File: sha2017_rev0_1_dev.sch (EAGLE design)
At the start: 79 parts, among them IC1 CP210X_USB_UART, IC2 AP7215, IC32 ESP32_AI, Q1 MMBT2222A, Q2 MMBT2222A, Q6 MOSFET-NCHANNELBSS123LT1G, SW801 MCMT5-F-V, X701 2908-05WB-MG

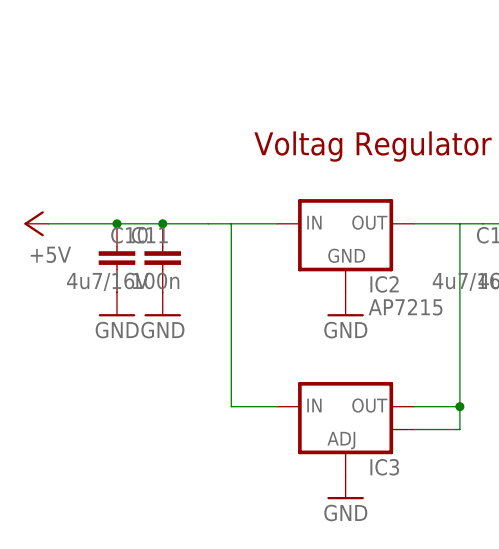
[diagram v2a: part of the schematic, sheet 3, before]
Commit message: all parts places minor adjustments needed
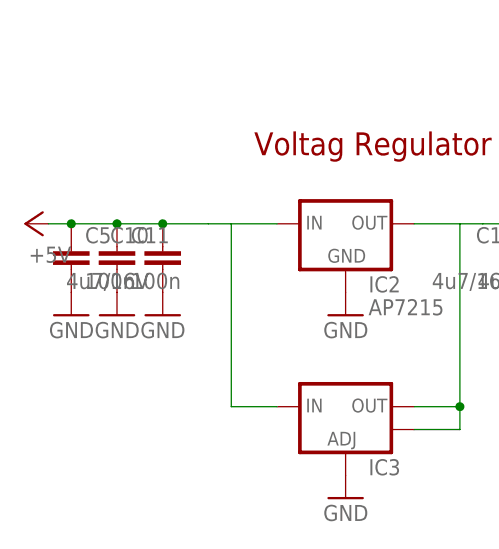
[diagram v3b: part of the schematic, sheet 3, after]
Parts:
- added C5: 100n, rcl:C-EUC0805
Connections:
- net +5V: now also C5.1
- net GND: now also C5.2
- net LCD_!RESET: now also SJ8.2; no longer SJ12.2
- net LCD_BUSY: now also SJ12.2; no longer SJ14.2
- net LCD_CS: now also SJ9.2; no longer SJ11.2
- net LCD_D/!S: now also SJ14.2; no longer SJ8.2
- net LCD_MOSI: now also SJ11.2; no longer SJ9.2
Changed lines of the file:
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@@
 <part name="GND15" library="supply1" deviceset="GND" device=""/>
 <part name="VDD5" library="supply1" deviceset="VDD" device=""/>
+<part name="C5" library="rcl" deviceset="C-EU" device="C0805" value="100n"/>
+<part name="GND14" library="supply1" deviceset="GND" device=""/>
 </parts>
 <sheets>
@@
 </segment>
 </net>
-<net name="LCD_D/!S" class="0">
-<segment>
-<label x="228.6" y="160.02" size="1.27" layer="95" xref="yes"/>
-<pinref part="SJ8" gate="G$1" pin="2"/>
-<wire x1="223.52" y1="160.02" x2="228.6" y2="160.02" width="0.1524" layer="91"/>
-</segment>
-</net>
-<net name="LCD_MOSI" class="0">
+<net name="LCD_SCK" class="0">
+<segment>
+<wire x1="218.44" y1="152.4" x2="228.6" y2="152.4" width="0.1524" layer="91"/>
+<label x="228.6" y="152.4" size="1.27" layer="95" xref="yes"/>
+<pinref part="SJ10" gate="G$1" pin="2"/>
+</segment>
+</net>
+<net name="LCD_CS" class="0">
 <segment>
 <label x="228.6" y="154.94" size="1.27" layer="95" xref="yes"/>
 <pinref part="SJ9" gate="G$1" pin="2"/>
 <wire x1="223.52" y1="154.94" x2="228.6" y2="154.94" width="0.1524" layer="91"/>
-</segment>
-</net>
-<net name="LCD_SCK" class="0">
-<segment>
-<wire x1="218.44" y1="152.4" x2="228.6" y2="152.4" width="0.1524" layer="91"/>
-<label x="228.6" y="152.4" size="1.27" layer="95" xref="yes"/>
-<pinref part="SJ10" gate="G$1" pin="2"/>
-</segment>
-</net>
-<net name="LCD_CS" class="0">
-<segment>
-<label x="228.6" y="149.86" size="1.27" layer="95" xref="yes"/>
-<pinref part="SJ11" gate="G$1" pin="2"/>
-<wire x1="223.52" y1="149.86" x2="228.6" y2="149.86" width="0.1524" layer="91"/>
 </segment>
 </net>
@@
 <net name="LCD_BUSY" class="0">
 <segment>
+<pinref part="SJ12" gate="G$1" pin="2"/>
+<wire x1="218.44" y1="162.56" x2="228.6" y2="162.56" width="0.1524" layer="91"/>
+<label x="228.6" y="162.56" size="1.27" layer="95" xref="yes"/>
+</segment>
+</net>
+<net name="LCD_!RESET" class="0">
+<segment>
+<label x="228.6" y="160.02" size="1.27" layer="95" xref="yes"/>
+<pinref part="SJ8" gate="G$1" pin="2"/>
+<wire x1="223.52" y1="160.02" x2="228.6" y2="160.02" width="0.1524" layer="91"/>
+</segment>
+</net>
+<net name="LCD_D/!S" class="0">
+<segment>
 <pinref part="SJ14" gate="G$1" pin="2"/>
 <wire x1="218.44" y1="157.48" x2="228.6" y2="157.48" width="0.1524" layer="91"/>
@@
 </segment>
 </net>
-<net name="LCD_!RESET" class="0">
-<segment>
-<pinref part="SJ12" gate="G$1" pin="2"/>
-<wire x1="218.44" y1="162.56" x2="228.6" y2="162.56" width="0.1524" layer="91"/>
-<label x="228.6" y="162.56" size="1.27" layer="95" xref="yes"/>
+<net name="LCD_MOSI" class="0">
+<segment>
+<label x="228.6" y="149.86" size="1.27" layer="95" xref="yes"/>
+<pinref part="SJ11" gate="G$1" pin="2"/>
+<wire x1="223.52" y1="149.86" x2="228.6" y2="149.86" width="0.1524" layer="91"/>
 </segment>
 </net>
@@
 <instance part="IC3" gate="G$1" x="157.48" y="119.38"/>
 <instance part="GND1" gate="1" x="157.48" y="109.22" rot="MR0"/>
+<instance part="C5" gate="G$1" x="127" y="137.16"/>
+<instance part="GND14" gate="1" x="127" y="129.54" rot="MR0"/>
 </instances>
 <busses>
@@
 <pinref part="IC3" gate="G$1" pin="ADJ"/>
 <pinref part="GND1" gate="1" pin="GND"/>
+</segment>
+<segment>
+<pinref part="C5" gate="G$1" pin="2"/>
+<pinref part="GND14" gate="1" pin="GND"/>
 </segment>
 </net>
@@
 <junction x="137.16" y="139.7"/>
 <pinref part="C11" gate="G$1" pin="1"/>
-<wire x1="132.08" y1="139.7" x2="124.46" y2="139.7" width="0.1524" layer="91"/>
+<wire x1="132.08" y1="139.7" x2="127" y2="139.7" width="0.1524" layer="91"/>
 <junction x="132.08" y="139.7"/>
+<wire x1="127" y1="139.7" x2="124.46" y2="139.7" width="0.1524" layer="91"/>
 <wire x1="142.24" y1="139.7" x2="144.78" y2="139.7" width="0.1524" layer="91"/>
 <pinref part="IC2" gate="G$1" pin="IN"/>
@@
 <pinref part="IC3" gate="G$1" pin="IN"/>
 <wire x1="144.78" y1="119.38" x2="149.86" y2="119.38" width="0.1524" layer="91"/>
-</segment>
-</net>
+<pinref part="C5" gate="G$1" pin="1"/>
+<junction x="127" y="139.7"/>
+</segment>
+</net>

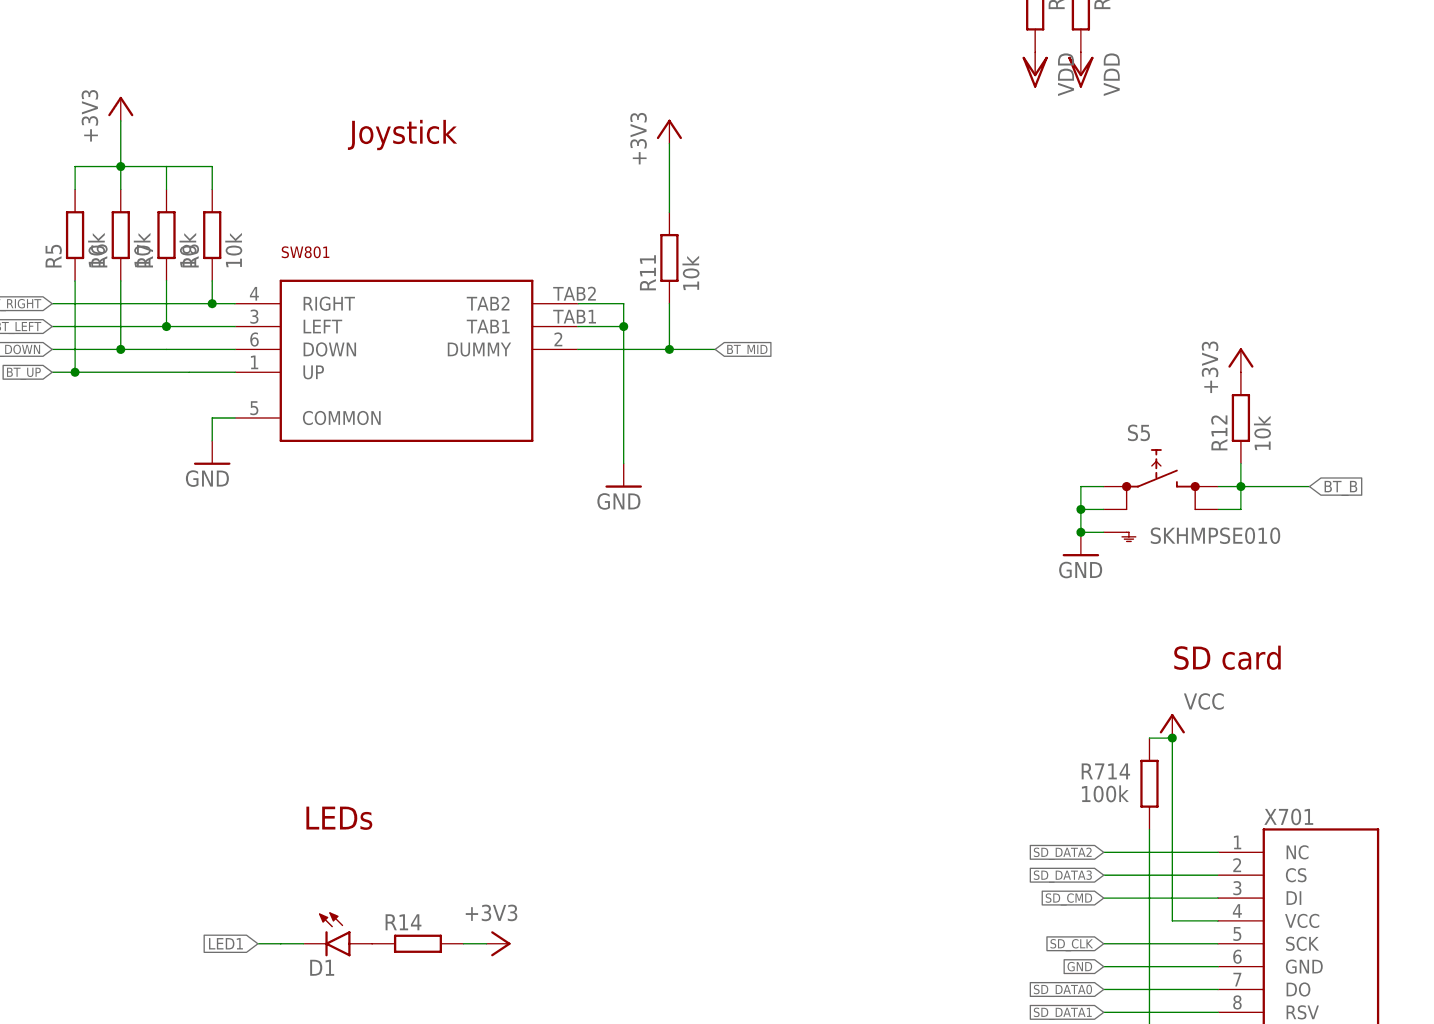
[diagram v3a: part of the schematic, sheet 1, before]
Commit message: finished routing. Part designators needs to be fixed
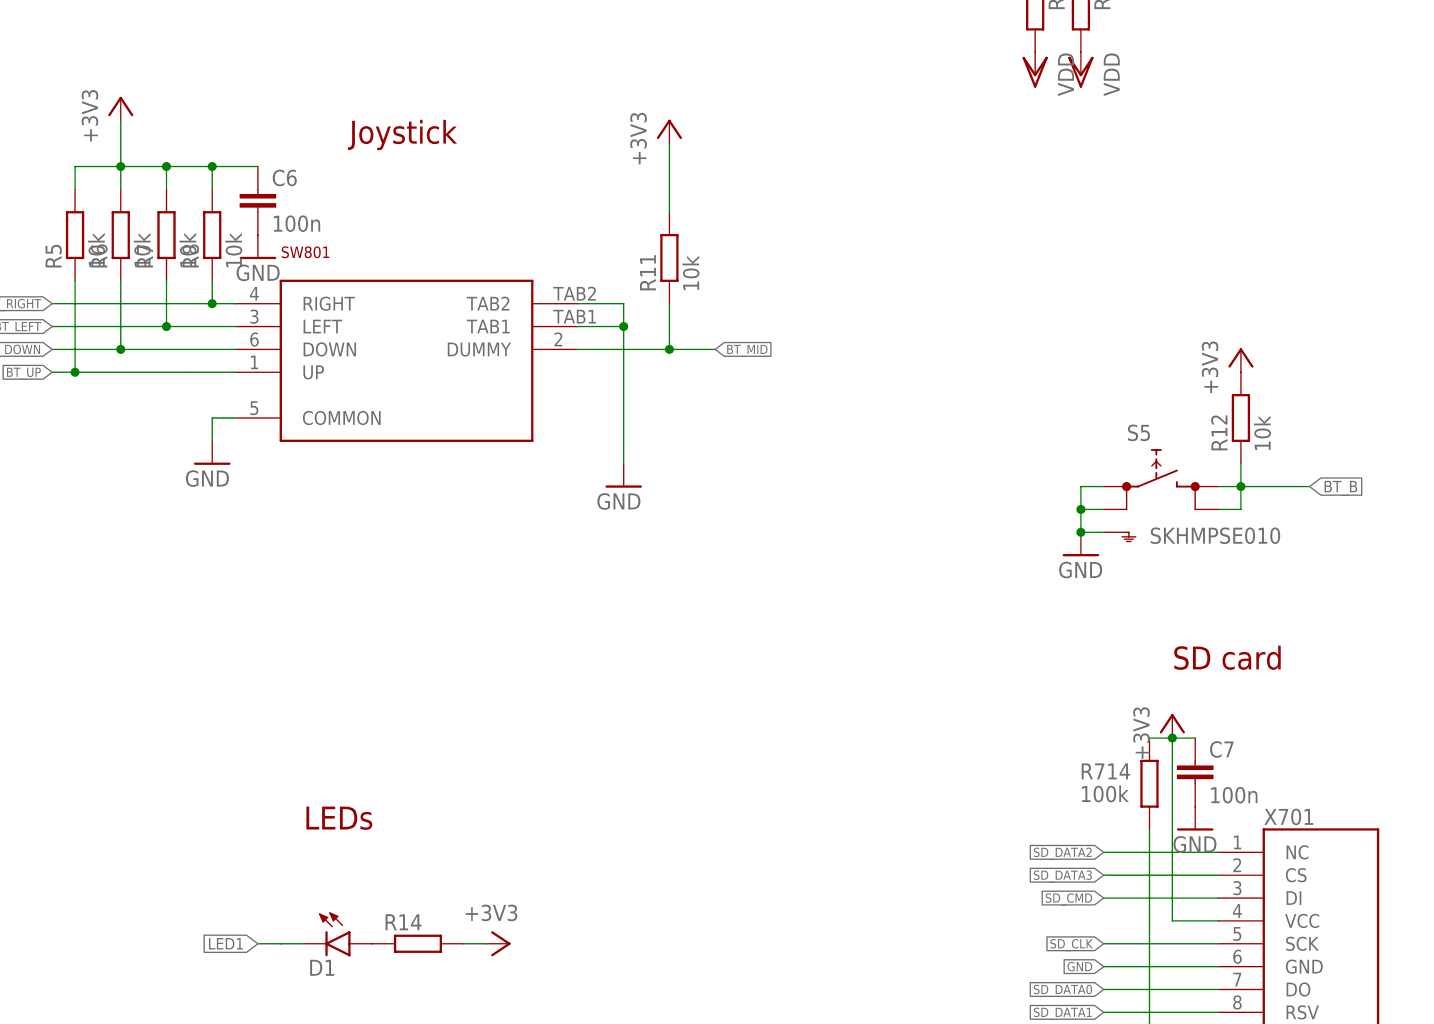
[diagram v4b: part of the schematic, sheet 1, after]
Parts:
- added C6, C7: 100n, rcl:C-EUC0603
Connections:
- removed net VCC: R714.1, X701.VCC
- net +3V3: now also C6.1, C7.1, R714.1, X701.VCC
- net BT_B: now also SJ7.1; no longer SJ2.1
- net BT_DOWN: now also SJ3.1; no longer SJ6.1
- net BT_MID: now also SJ6.1; no longer SJ7.1
- net BT_RIGHT: now also SJ2.1; no longer SJ5.1
- net BT_UP: now also SJ5.1; no longer SJ3.1
- net GND: now also C6.2, C7.2
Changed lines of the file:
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@@
 </part>
 <part name="GND59" library="supply1" deviceset="GND" device=""/>
-<part name="P+14" library="supply1" deviceset="VCC" device=""/>
 <part name="R714" library="rcl" deviceset="R-EU_" device="R0603" value="100k"/>
 <part name="D2" library="SparkFun-LED" deviceset="LED" device="0603"/>
@@
 <part name="C5" library="rcl" deviceset="C-EU" device="C0805" value="100n"/>
 <part name="GND14" library="supply1" deviceset="GND" device=""/>
+<part name="+3V7" library="supply1" deviceset="+3V3" device=""/>
+<part name="C6" library="rcl" deviceset="C-EU" device="C0603" value="100n"/>
+<part name="GND16" library="supply1" deviceset="GND" device=""/>
+<part name="C7" library="rcl" deviceset="C-EU" device="C0603" value="100n"/>
+<part name="GND17" library="supply1" deviceset="GND" device=""/>
 </parts>
 <sheets>
@@
 <attribute name="VALUE" x="160.02" y="21.59" size="1.778" layer="96" rot="R270"/>
 </instance>
-<instance part="P+14" gate="VCC" x="162.56" y="76.2" smashed="yes">
-<attribute name="VALUE" x="163.83" y="76.835" size="1.778" layer="96"/>
-</instance>
 <instance part="R714" gate="G$1" x="160.02" y="68.58" smashed="yes" rot="R270">
 <attribute name="NAME" x="152.273" y="69.0626" size="1.778" layer="95"/>
@@
 <instance part="GND15" gate="1" x="86.36" y="220.98" rot="MR0"/>
 <instance part="VDD5" gate="G$1" x="154.94" y="203.2" rot="R270"/>
+<instance part="+3V7" gate="G$1" x="162.56" y="76.2"/>
+<instance part="C6" gate="G$1" x="60.96" y="134.62"/>
+<instance part="GND16" gate="1" x="60.96" y="127" rot="MR0"/>
+<instance part="C7" gate="G$1" x="165.1" y="71.12"/>
+<instance part="GND17" gate="1" x="165.1" y="63.5"/>
 </instances>
 <busses>
@@
 <wire x1="86.36" y1="226.06" x2="86.36" y2="223.52" width="0.1524" layer="91"/>
 <pinref part="GND15" gate="1" pin="GND"/>
+</segment>
+<segment>
+<pinref part="C6" gate="G$1" pin="2"/>
+<pinref part="GND16" gate="1" pin="GND"/>
+</segment>
+<segment>
+<pinref part="C7" gate="G$1" pin="2"/>
+<pinref part="GND17" gate="1" pin="GND"/>
 </segment>
 </net>
@@
 <wire x1="45.72" y1="137.16" x2="45.72" y2="142.24" width="0.1524" layer="91"/>
 <pinref part="+3V4" gate="G$1" pin="+3V3"/>
+<pinref part="C6" gate="G$1" pin="1"/>
+<wire x1="55.88" y1="137.16" x2="60.96" y2="137.16" width="0.1524" layer="91"/>
+<junction x="50.8" y="137.16"/>
+<junction x="55.88" y="137.16"/>
 </segment>
 <segment>
@@
 <wire x1="83.82" y1="50.8" x2="86.36" y2="50.8" width="0.1524" layer="91"/>
 <pinref part="+2V2" gate="G$1" pin="+3V3"/>
+</segment>
+<segment>
+<pinref part="X701" gate="G$1" pin="VCC"/>
+<wire x1="162.56" y1="73.66" x2="162.56" y2="53.34" width="0.1524" layer="91"/>
+<wire x1="162.56" y1="53.34" x2="167.64" y2="53.34" width="0.1524" layer="91"/>
+<pinref part="R714" gate="G$1" pin="1"/>
+<wire x1="160.02" y1="73.66" x2="162.56" y2="73.66" width="0.1524" layer="91"/>
+<pinref part="+3V7" gate="G$1" pin="+3V3"/>
+<junction x="162.56" y="73.66"/>
+<pinref part="C7" gate="G$1" pin="1"/>
+<wire x1="162.56" y1="73.66" x2="165.1" y2="73.66" width="0.1524" layer="91"/>
 </segment>
 </net>
@@
 <pinref part="D1" gate="G$1" pin="A"/>
 <pinref part="R14" gate="G$1" pin="1"/>
-</segment>
-</net>
-<net name="VCC" class="1">
-<segment>
-<pinref part="P+14" gate="VCC" pin="VCC"/>
-<pinref part="X701" gate="G$1" pin="VCC"/>
-<wire x1="162.56" y1="73.66" x2="162.56" y2="53.34" width="0.1524" layer="91"/>
-<wire x1="162.56" y1="53.34" x2="167.64" y2="53.34" width="0.1524" layer="91"/>
-<pinref part="R714" gate="G$1" pin="1"/>
-<wire x1="160.02" y1="73.66" x2="162.56" y2="73.66" width="0.1524" layer="91"/>
-<junction x="162.56" y="73.66"/>
 </segment>
 </net>
@@
 </segment>
 </net>
-<net name="BT_B" class="0">
+<net name="BT_LEFT" class="0">
+<segment>
+<pinref part="SJ4" gate="G$1" pin="1"/>
+<wire x1="116.84" y1="154.94" x2="114.3" y2="154.94" width="0.1524" layer="91"/>
+<label x="114.3" y="154.94" size="1.27" layer="95" rot="R180" xref="yes"/>
+</segment>
+</net>
+<net name="BT_DOWN" class="0">
+<segment>
+<pinref part="SJ3" gate="G$1" pin="1"/>
+<wire x1="124.46" y1="157.48" x2="114.3" y2="157.48" width="0.1524" layer="91"/>
+<label x="114.3" y="157.48" size="1.27" layer="95" rot="R180" xref="yes"/>
+</segment>
+</net>
+<net name="BT_RIGHT" class="0">
 <segment>
 <pinref part="SJ2" gate="G$1" pin="1"/>
@@
 </segment>
 </net>
-<net name="BT_UP" class="0">
-<segment>
-<pinref part="SJ3" gate="G$1" pin="1"/>
-<wire x1="124.46" y1="157.48" x2="114.3" y2="157.48" width="0.1524" layer="91"/>
-<label x="114.3" y="157.48" size="1.27" layer="95" rot="R180" xref="yes"/>
-</segment>
-</net>
-<net name="BT_LEFT" class="0">
-<segment>
-<pinref part="SJ4" gate="G$1" pin="1"/>
-<wire x1="116.84" y1="154.94" x2="114.3" y2="154.94" width="0.1524" layer="91"/>
-<label x="114.3" y="154.94" size="1.27" layer="95" rot="R180" xref="yes"/>
-</segment>
-</net>
-<net name="BT_DOWN" class="0">
+<net name="BT_MID" class="0">
 <segment>
 <pinref part="SJ6" gate="G$1" pin="1"/>
 <wire x1="124.46" y1="152.4" x2="114.3" y2="152.4" width="0.1524" layer="91"/>
 <label x="114.3" y="152.4" size="1.27" layer="95" rot="R180" xref="yes"/>
-</segment>
-</net>
-<net name="BT_RIGHT" class="0">
-<segment>
-<pinref part="SJ5" gate="G$1" pin="1"/>
-<wire x1="116.84" y1="149.86" x2="114.3" y2="149.86" width="0.1524" layer="91"/>
-<label x="114.3" y="149.86" size="1.27" layer="95" rot="R180" xref="yes"/>
-</segment>
-</net>
-<net name="BT_MID" class="0">
-<segment>
-<pinref part="SJ7" gate="G$1" pin="1"/>
-<wire x1="124.46" y1="147.32" x2="114.3" y2="147.32" width="0.1524" layer="91"/>
-<label x="114.3" y="147.32" size="1.27" layer="95" rot="R180" xref="yes"/>
 </segment>
 </net>
@@
 </segment>
 </net>
+<net name="BT_UP" class="0">
+<segment>
+<pinref part="SJ5" gate="G$1" pin="1"/>
+<wire x1="116.84" y1="149.86" x2="114.3" y2="149.86" width="0.1524" layer="91"/>
+<label x="114.3" y="149.86" size="1.27" layer="95" rot="R180" xref="yes"/>
+</segment>
+</net>
+<net name="BT_B" class="0">
+<segment>
+<pinref part="SJ7" gate="G$1" pin="1"/>
+<wire x1="124.46" y1="147.32" x2="114.3" y2="147.32" width="0.1524" layer="91"/>
+<label x="114.3" y="147.32" size="1.27" layer="95" rot="R180" xref="yes"/>
+</segment>
+</net>
